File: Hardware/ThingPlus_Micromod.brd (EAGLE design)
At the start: 90.2 x 22.9 mm, 68 parts, among them J4 QWIIC_RIGHT_ANGLE, J5 MICRO-SD-SDIOPUSH-PUSH, J6 CORTEX_DEBUG, J7 MICROMOD-2222-C, U1 74LVC1G04SE, U2 MCP73831, U3 MAX17048, U4 3.3V, U5 3.3V

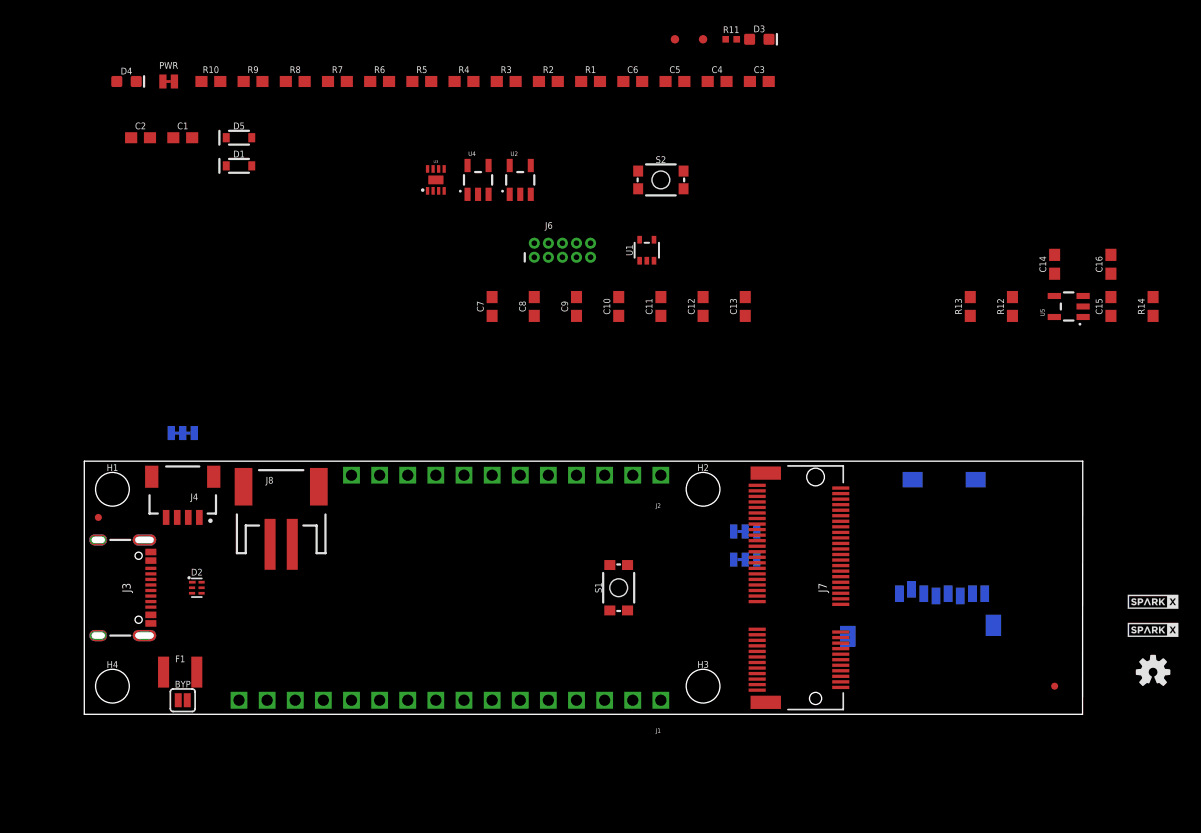
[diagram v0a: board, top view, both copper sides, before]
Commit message: Update SPI net names
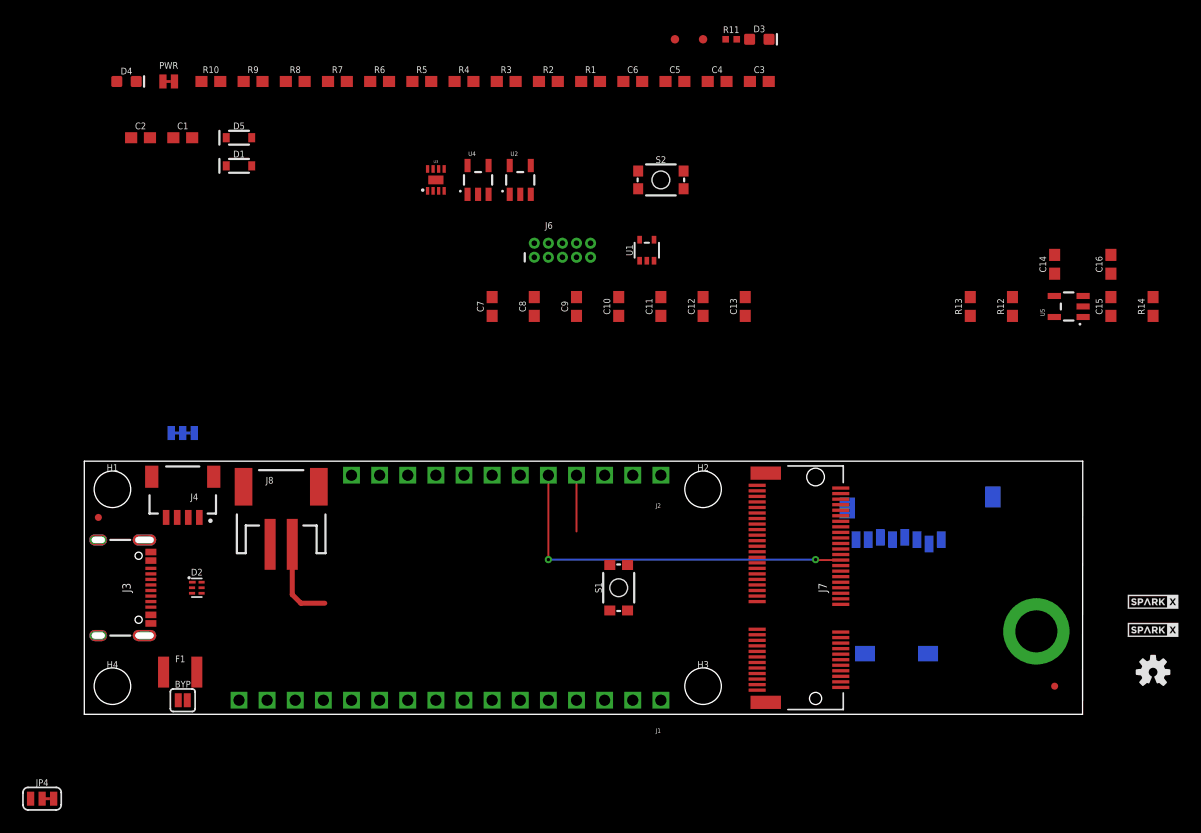
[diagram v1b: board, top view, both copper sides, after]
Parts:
- removed JP2, JP3: JUMPER-SMT_3_1-NC_TRACE_SILK, SparkFun-Jumpers:SMT-JUMPER_3_1-NC_TRACE_SILK
- added H5: STAND-OFF-REFLOW2.5MM_TALL, SparkFun-Hardware:STAND-OFF-REFLOW-M2.5
- added JP4: JUMPER-SMT_3_1-NC_TRACE_SILK, SparkFun-Jumpers:SMT-JUMPER_3_1-NC_TRACE_SILK
- H1, H2, H3, H4: value STAND-OFFTIGHT -> STAND-OFF; device SparkFun-Hardware:STAND-OFF-TIGHT -> SparkFun-Hardware:STAND-OFF
- J3: device SparkFun-Connectors:USB-C-16P_4LAYER-PADS -> SparkFun-Connectors:USB-C-16P-2LAYER-PADS
- moved J5 21.7 mm to (68.5, 5.08), turned to 0 degrees
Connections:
- net !SPI_CS! renamed !SD_CS!
- removed net A2: J1.10, J7.40
- removed net A3: J1.9, J7.42
- removed net A4: J1.8, J7.44
- removed net A5: J1.7, J7.46
- removed net D10: J2.6, J7.73
- removed net D11: J2.7, J7.48
- removed net D12: J2.8, JP2.2
- removed net D13: J2.9, JP3.2
- removed net D5: J2.3, J7.67
- removed net D6: J2.4, J7.69
- removed net D9: J2.5, J7.71
- removed net MISO: J1.4
- removed net MOSI: J1.5
- removed net N$1: R14.1, U5.3
- removed net SCK: J1.6
- removed net SPI_SDI: J5.DI/CMD, J7.61
- removed net SPI_SDO: J5.DO/DAT0, J7.59
- new net G0: J2.9, J7.40
- new net G1: J2.8, J7.42
- new net G2: J2.7, J7.44
- new net G3: J2.6, J7.46
- new net G4: J2.5, J7.48
- new net G5: J2.4, J7.73
- new net G6: J2.3, J7.71
- new net G7: J7.69, JP4.1
- new net N$5: J2.2, JP4.2
- new net SCL/G7: J4.4, R3.1
- new net SPI_CIPO: J1.4, J5.DO/DAT0, J7.61
- new net SPI_COPI: J1.5, J5.DI/CMD, J7.59
- net 3.3V: now also R10.2
- net D0: now also J1.8; no longer JP2.1
- net D1: now also J1.7; no longer JP3.1
- net EN: now also R14.1, U5.3; no longer J7.4
- net GND: now also H5.1
- net PWM0: now also J1.10; no longer JP2.3
- net PWM1: now also J1.9; no longer JP3.3
- net SCL: now also JP4.3; no longer J2.2, J4.4, R3.1
- net SPI_SCK: now also J1.6
- net VIN: no longer R10.2
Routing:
- net G4: track 0.00 -> 34.0 mm, vias 0 -> 2
- net V_BATT: track 0.00 -> 7.80 mm
- net G5: track 0.00 -> 5.08 mm

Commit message: Corrected schematic, board layout WIP
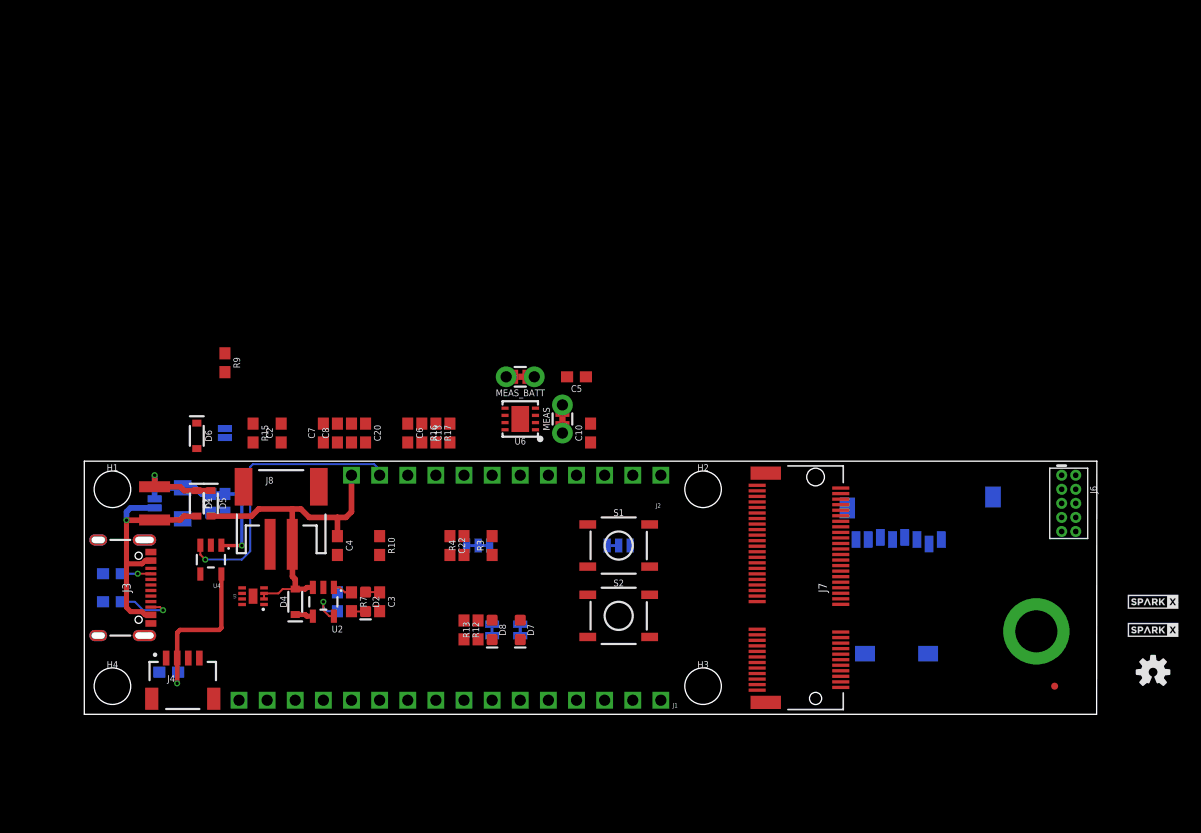
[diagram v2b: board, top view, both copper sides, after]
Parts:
- removed BYP: JUMPER-SMT_2_NO_SILK, SparkFun-Jumpers:SMT-JUMPER_2_NO_SILK
- removed C1, C12, C16, C9: 0.1uF, SparkFun-Capacitors:0603
- removed C14, C15: 1.0uF, SparkFun-Capacitors:0603
- removed D3: RED, SparkFun-LED:LED-0603
- removed F1: 6V/2A, SparkFun-Fuses:1210
- removed FD1: FIDUCIALUFIDUCIAL, SparkFun-Aesthetics:FIDUCIAL-MICRO
- removed PWR: (no value), SparkFun-Jumpers:SMT-JUMPER_2_NC_TRACE_NO-SILK
- removed R11: 1k, SparkFun-Resistors:0402-TIGHT
- removed R14: 10k, SparkFun-Resistors:0603
- removed R5: 5.1k, SparkFun-Resistors:0603
- removed R8: 1k, SparkFun-Resistors:0603
- removed TP1, TP2: (no value), SparkFun-Connectors:PAD.03X.03
- removed U1: 74LVC1G04SE, SparkFun-IC-Logic:SOT353
- removed U5: 3.3V, SparkFun-IC-Power:SOT23-5
- added 3V3_LED, VIN_LED: (no value), SparkFun-Jumpers:SMT-JUMPER_2_NC_TRACE_SILK
- added BYP1: JUMPER-SMT_2_NO_SILK, SparkFun-Jumpers:SMT-JUMPER_2_NO_SILK
- added C17, C22: 0.22uF, SparkFun-Capacitors:0603
- added C18, C21: 0.1uF, SparkFun-Capacitors:0603
- added C19: 10uF, SparkFun-Capacitors:EIA3216
- added C20: 1.0uF, SparkFun-Capacitors:0603
- added D6: 3.3V, SparkFun-DiscreteSemi:SOD-323
- added D7: RED, SparkFun-LED:LED-0603
- added D8: Yellow, SparkFun-LED:LED-0603
- added F2: 6V/2A, SparkFun-Fuses:1210
- added MEAS, MEAS_BATT: (no value), SparkFun-Jumpers:COMBO-JUMPER_2_NC_TRACE
- added R15: 100k, SparkFun-Resistors:0603
- added R16: 1k, SparkFun-Resistors:0603
- added R17: 4.7k, SparkFun-Resistors:0603
- added U6: AP7361C-33, SparkFun-IC-Power:UDFN-8
- added VE: (no value), SparkFun-Jumpers:SMT-JUMPER_2_NO_SILK
- D2: value PRTR5V0U2F -> Yellow; device SparkFun-IC-Power:SOT886 -> SparkFun-LED:LED-0603
- D4: value Yellow -> 3A/10V/280mV; device SparkFun-LED:LED-0603 -> SparkFun-DiscreteSemi:SOD-323
- J6: value CORTEX_DEBUG -> JTAG; device SparkFun-Connectors:2X5-PTH-1.27MM-NO_SILK -> SparkFun-Connectors:2X5-PTH-1.27MM
- R1: value 4.7k -> 5.1k
- R10: value 10k -> 100k
- R12: value 5.1k -> 20k
- R13: value 9.76k -> 10k
- R2: value 10k -> 5.1k
- R6: value 5.1k -> 2.2k
- R7: value 2.0k -> 1k
- S1: value MOMENTARY-SWITCH-SPST-SMD-4.6X2.8MM -> Reset; device SparkFun-Switches:TACTILE_SWITCH_SMD_4.6X2.8MM -> SparkFun-Switches:TACTILE_SWITCH_SMD_5.2MM
- S2: value MOMENTARY-SWITCH-SPST-SMD-4.6X2.8MM -> BOOT; device SparkFun-Switches:TACTILE_SWITCH_SMD_4.6X2.8MM -> SparkFun-Switches:TACTILE_SWITCH_SMD_5.2MM
- U4: device SparkFun-IC-Power:SOT23-5 -> SparkFun-IC-Power:SOT23-5@1
- moved R1 63.8 mm to (2.54, 10.2), flipped to the bottom, turned to 180 degrees
- moved R2 59.4 mm to (2.54, 12.7), flipped to the bottom, turned to 180 degrees
- moved C3 58.2 mm to (26.7, 10.2), turned to 270 degrees
- moved R12 57.5 mm to (34.3, 7.62), turned to 270 degrees
- moved JP4 56.9 mm to (48.3, 15.2), flipped to the bottom
- moved C11 55.4 mm to (7.62, 3.81), flipped to the bottom, turned to 0 degrees
- moved C4 54.2 mm to (22.9, 15.2), turned to 270 degrees
- moved R13 53.2 mm to (35.6, 7.62)
- moved J6 51.1 mm to (88.9, 19.1), turned to 270 degrees
- moved D4 49.4 mm to (19.1, 10.2), turned to 90 degrees
- moved R6 47.1 mm to (22.9, 10.2), flipped to the bottom, turned to 270 degrees
- moved R7 47.0 mm to (24.1, 10.2), turned to 270 degrees
- moved R10 44.6 mm to (26.7, 15.2), turned to 270 degrees
- moved U2 42.0 mm to (21.6, 10.2), turned to 180 degrees
- moved R3 41.9 mm to (36.8, 15.2), turned to 90 degrees
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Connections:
- removed net !RESET: J6.10
- removed net 5V_RAW: BYP.1, F1.1, J3.VBUS1, J3.VBUS2
- removed net CC1: J3.A5, R5.2
- removed net CC2: J3.B5, R6.2
- removed net D+_RAW: D2.3, J3.A6, J3.B6
- removed net D-_RAW: D2.1, J3.A7, J3.B7
- removed net N$15: R8.1, U2.1
- removed net N$2: PWR.1, R11.2
- removed net N$7: D3.A, R11.1
- new net 3.3V_EN: J7.4, VE.1
- new net 3.3V_EN_VE: D6.C, R15.1, U6.5, VE.2
- new net 5V: C3.1, D2.A, D4.C, MEAS_BATT.1, MEAS_BATT.3, U2.4
- new net CHG_LED: R7.1, U2.1
- new net N$1: MEAS.1, MEAS.3, U6.1
- new net N$10: R17.2, VIN_LED.1
- new net N$11: D8.A, R17.1
- new net N$12: J3.A5, R2.2
- new net N$13: J3.B5, R1.2
- new net N$6: 3V3_LED.1, R16.2
- new net N$9: D7.A, R16.1
- net !BOOT!: now also S2.3, S2.4; no longer U1.4
- net !RESET!: now also J6.10; no longer C1.2, R1.1
- net 3.3V: now also 3V3_LED.2, C20.1, C21.1, C22.1, MEAS.2, MEAS.4; no longer C12.1, C15.1, C16.1, PWR.2, R1.2, S2.3, S2.4, U1.5, U5.5
- net BOOT0: no longer R2.2, S2.1, S2.2, U1.2
- net EN: no longer R14.1, U5.3
- net GND: now also C17.2, C18.2, C19.-, C20.2, C21.2, C22.2, D6.A, D7.C, D8.C, R1.1, S2.1, S2.2, U6.4, U6.EP; no longer C1.1, C12.2, C14.2, C15.2, C16.2, C9.2, D2.2, D3.C, J3.SHLD1, J3.SHLD2, J3.SHLD3, J3.SHLD4, R5.1, R7.1, U1.3, U5.2
- net N$14: now also D2.C, R7.2; no longer D4.C, R8.2
- net N$8: now also R6.2; no longer R7.2
- net SWDCK: no longer TP2.P$1
- net SWDIO: no longer TP1.P$1
- net USB_D+: now also J3.A6, J3.B6; no longer D2.4
- net USB_D-: now also J3.A7, J3.B7; no longer D2.6
- net VIN: now also BYP1.2, C17.1, C18.1, C19.+, F2.2, MEAS_BATT.2, MEAS_BATT.4, R15.2, U6.8, VIN_LED.2; no longer C14.1, R14.2, U5.1
- net V_BATT: now also D4.A; no longer C9.1
- net V_USB: now also BYP1.1, F2.1, J3.VBUS1, J3.VBUS2; no longer BYP.2, C3.1, D2.5, D4.A, F1.2, U2.4
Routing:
- net G4: track 34.0 -> 0.00 mm, vias 2 -> 0
- net EN: track 0.00 -> 26.0 mm, vias 0 -> 1
- net V_BATT: track 7.80 -> 31.0 mm
- net VIN: track 0.00 -> 23.0 mm, vias 0 -> 2
- net V_USB: track 0.00 -> 22.7 mm, vias 0 -> 1
- net QWIIC_PWR: track 0.00 -> 14.7 mm, vias 0 -> 1
- net N$13: track 0.00 -> 5.26 mm, vias 0 -> 1
- net G5: track 5.08 -> 0.00 mm
- net N$8: track 0.00 -> 3.85 mm, vias 0 -> 1
- net 5V: track 0.00 -> 2.93 mm
- net N$12: track 0.00 -> 2.63 mm, vias 0 -> 1
- net CHG_LED: track 0.00 -> 1.78 mm
- net N$14: track 0.00 -> 1.28 mm
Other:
- board size 90.2 x 22.9 mm -> 91.4 x 22.9 mm

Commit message: ThingPlus Micromod board routing WIP
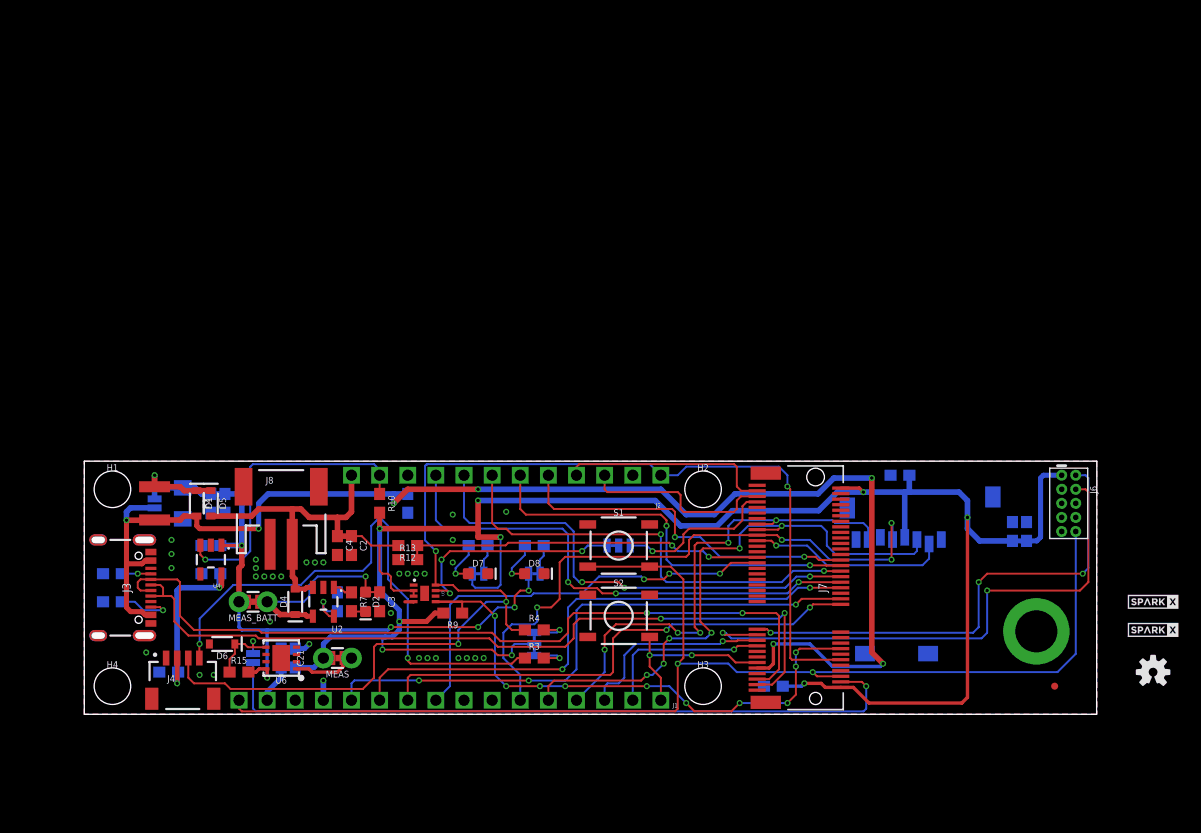
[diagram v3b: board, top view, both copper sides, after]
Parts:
- moved C7 64.1 mm to (85.1, 16.5), flipped to the bottom, turned to 270 degrees
- moved C8 61.6 mm to (83.8, 16.5), flipped to the bottom, turned to 270 degrees
- moved C13 40.8 mm to (73.7, 21.6), flipped to the bottom, turned to 0 degrees
- moved C5 36.4 mm to (11.4, 15.2), flipped to the bottom, turned to 0 degrees
- moved C22 31.9 mm to (62.2, 2.54), flipped to the bottom, turned to 0 degrees
- moved MEAS_BATT 31.5 mm to (15.2, 10.2)
- moved R9 30.6 mm to (33.3, 9.14), turned to 180 degrees
- moved U6 30.5 mm to (17.8, 5.08)
- moved MEAS 29.6 mm to (22.9, 5.08), turned to 180 degrees
- moved C6 21.8 mm to (11.4, 12.7), flipped to the bottom, turned to 0 degrees
- moved C20 21.7 mm to (17.8, 5.08), flipped to the bottom, turned to 90 degrees
- moved R15 21.6 mm to (14.0, 3.81), turned to 0 degrees
- moved C21 20.9 mm to (19.1, 5.08), flipped to the bottom, turned to 90 degrees
- moved VE 20.5 mm to (15.2, 5.08)
- moved D6 18.9 mm to (12.4, 6.35), turned to 180 degrees
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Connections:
- removed net BOOT0: J1.1
- net !BOOT!: now also J1.1
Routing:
- net 3.3V: track 0.00 -> 175.9 mm, vias 0 -> 9
- net SDA: track 0.00 -> 114.1 mm, vias 0 -> 4
- net !RESET!: track 0.00 -> 112.3 mm, vias 0 -> 2
- net V_USB: track 22.7 -> 123.7 mm, vias 1 -> 7
- net USB_D-: track 0.02 -> 73.0 mm, vias 0 -> 2
- net USB_D+: track 0.01 -> 72.6 mm, vias 0 -> 2
- net 3.3V_EN: track 0.00 -> 64.2 mm, vias 0 -> 1
- net SPI_SCK: track 0.00 -> 54.6 mm, vias 0 -> 4
- net SPI_COPI: track 0.00 -> 53.4 mm, vias 0 -> 6
- net A0: track 0.00 -> 52.0 mm, vias 0 -> 3
- net !I2C_INT!: track 0.00 -> 51.8 mm, vias 0 -> 10
- net SCL/G7: track 0.00 -> 50.2 mm, vias 0 -> 2
- net SWDCK: track 0.00 -> 50.1 mm, vias 0 -> 2
- net A1: track 0.00 -> 50.0 mm, vias 0 -> 2
- net G0: track 0.00 -> 46.3 mm, vias 0 -> 3
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- added copper zone on layer 1, net GND
- added copper zone on layer 16, net GND

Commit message: Preliminary version of routed board.
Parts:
- added FD1: FIDUCIALUFIDUCIAL, SparkFun-Aesthetics:FIDUCIAL-MICRO
- J3: device SparkFun-Connectors:USB-C-16P-2LAYER-PADS -> SparkFun-Connectors:USB-C-16P_4LAYER-PADS
- moved J6 19.4 mm to (78.7, 2.54), flipped to the bottom, turned to 0 degrees
- moved C20 17.3 mm to (31.8, 15.2), flipped to the top
- moved U6 16.1 mm to (33.0, 10.2), turned to 0 degrees
- moved C21 15.3 mm to (30.5, 15.2), flipped to the top
- moved C13 13.7 mm to (86.4, 16.5), turned to 90 degrees
- moved R9 11.2 mm to (44.5, 10.2), turned to 270 degrees
- moved U3 11.2 mm to (41.9, 10.2), turned to 0 degrees
- moved C22 10.2 mm to (72.4, 2.54), turned to 180 degrees
- moved R15 9.25 mm to (22.9, 6.35)
- moved MEAS 8.13 mm to (29.2, 10.2), turned to 90 degrees
- moved D6 6.60 mm to (19.1, 6.35)
- moved VE 6.48 mm to (21.6, 6.35)
- moved R3 5.24 mm to (39.4, 10.2), turned to 90 degrees
- moved C6 5.24 mm to (10.2, 7.62), flipped to the top, turned to 180 degrees
- moved R4 4.58 mm to (36.8, 10.2), turned to 90 degrees
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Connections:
- net GND: now also J3.SHLD1, J3.SHLD2, J3.SHLD3, J3.SHLD4
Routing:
- net 3.3V: track 175.9 -> 45.8 mm, vias 9 -> 7
- net GND: track 4.01 -> 54.3 mm, vias 34 -> 56
- net D0: track 0.00 -> 45.2 mm, vias 0 -> 4
- net D1: track 0.00 -> 37.4 mm, vias 0 -> 1
- net SWDCK: track 50.1 -> 22.3 mm, vias 2 -> 1
- net SPI_CIPO: track 45.1 -> 70.9 mm, vias 5 -> 2
- net SCL: track 20.2 -> 43.5 mm, vias 3 -> 2
- net 3.3V_EN_VE: track 7.33 -> 28.3 mm
- net SWDIO: track 44.2 -> 25.5 mm, vias 3 -> 1
- net V_BATT: track 40.6 -> 59.1 mm, vias 0 -> 2
- net !I2C_INT!: track 51.8 -> 33.7 mm, vias 10 -> 2
- net !RESET!: track 112.3 -> 95.4 mm
- net 3.3V_EN: track 64.2 -> 49.9 mm, vias 1 -> 2
- net SCL/G7: track 50.2 -> 36.4 mm, vias 2 -> 3
- net V_USB: track 123.7 -> 111.2 mm, vias 7 -> 4
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- added copper zone on layer 15, net 3.3V
- added copper zone on layer 2, net GND
- added copper zone on layer 15, net VIN
- added copper zone on layer 15, net V_USB
